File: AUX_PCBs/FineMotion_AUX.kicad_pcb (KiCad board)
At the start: 2 copper layers, 49.9 x 19.4 mm, 14 parts, among them J2 Conn_01x04_Female, U1 ME6211C, U9 MPU-9250

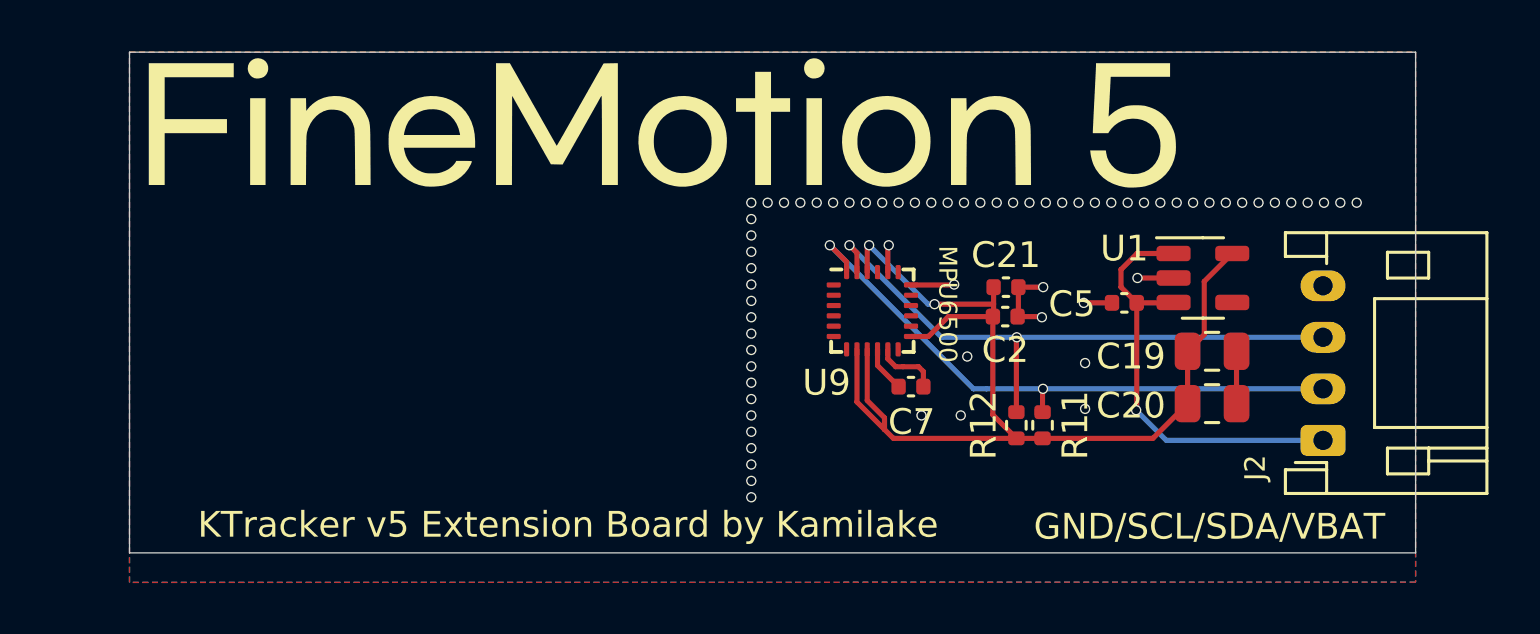
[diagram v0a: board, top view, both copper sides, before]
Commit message: Placement of pads to assemble the BNO085 module
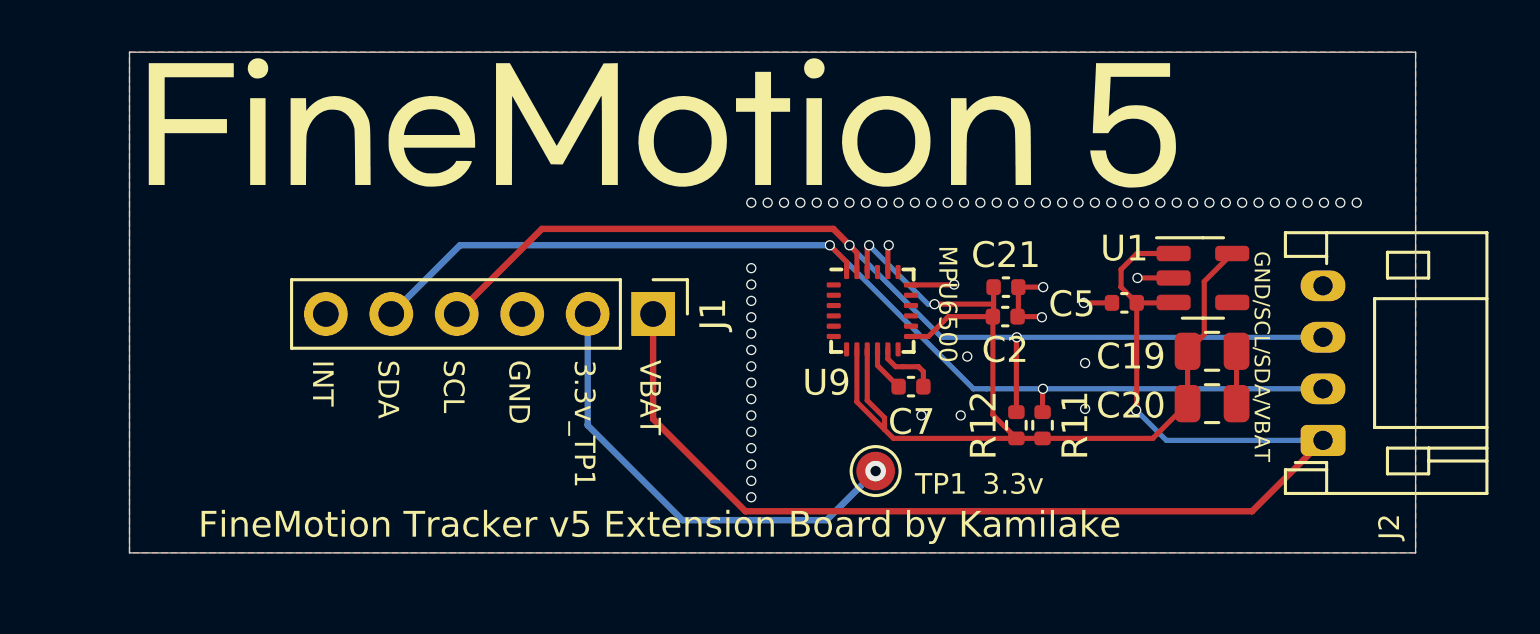
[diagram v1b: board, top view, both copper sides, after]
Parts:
- added J1: Conn_01x06_Male, Connector_PinHeader_2.54mm:PinHeader_1x06_P2.54mm_Vertical, F.Cu at (110.5, 65.9)
- added TP1: I2C_PULLUP, TestPoint:TestPoint_Pad_D1.5mm, F.Cu at (119.1, 72.0)
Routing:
- net VBAT: track 17.2 -> 49.9 mm
- net SDA: track 23.7 -> 41.8 mm
- net Net-(J1-Pad2): track 0.00 -> 17.8 mm, vias 0 -> 1
- net SCL: track 23.9 -> 40.8 mm
- net GND: vias 67 -> 64
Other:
- board text added: "3.3v"
- board text added: "3.3v_TP1"
- board text added: "FineMotion Tracker v5 Extension Board by Kamilake"
- board text added: "GND"
- board text added: "INT"
- board text added: "SCL"
- board text added: "SDA"
- board text added: "VBAT"
- board text removed: "KTracker v5 Extension Board by Kamilake"

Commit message: Premium logo~
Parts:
- G***: value LOGO -> FineMotion5
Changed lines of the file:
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@@
       (effects (font (size 1.524 1.524) (thickness 0.3)))
     )
-    (fp_text value "LOGO" (at 0.75 0) (layer "F.Adhes") hide
+    (fp_text value "FineMotion5" (at 0.75 0) (layer "F.SilkS") hide
       (effects (font (size 1.524 1.524) (thickness 0.3)))
     )
@@
         (xy 16.933333 -2.240139)
         (xy 19.808472 -2.240139)
-      ) (layer "F.SilkS") (width 0) (fill solid))
+      ) (layer "F.Mask") (width 0) (fill solid))
     (fp_poly (pts
         (xy -15.292917 2.487083)
@@
         (xy -15.892639 -0.881945)
         (xy -15.292917 -0.881945)
-      ) (layer "F.SilkS") (width 0) (fill solid))
+      ) (layer "F.Mask") (width 0) (fill solid))
     (fp_poly (pts
         (xy 1.142024 -0.954211)
@@
         (xy 0.742736 -0.959994)
         (xy 0.948969 -0.968346)
-      ) (layer "F.SilkS") (width 0) (fill solid))
+      ) (layer "F.Mask") (width 0) (fill solid))
     (fp_poly (pts
         (xy -8.663804 -0.959525)
@@
         (xy -9.128181 -0.944226)
         (xy -8.896952 -0.966529)
-      ) (layer "F.SilkS") (width 0) (fill solid))
+      ) (layer "F.Mask") (width 0) (fill solid))
     (fp_poly (pts
         (xy -12.428672 -0.960067)
@@
         (xy -12.847275 -0.945323)
         (xy -12.639255 -0.966713)
-      ) (layer "F.SilkS") (width 0) (fill solid))
+      ) (layer "F.Mask") (width 0) (fill solid))
     (fp_poly (pts
         (xy 6.087764 -2.422808)
@@
         (xy 5.8616 -2.409532)
         (xy 5.976982 -2.431571)
-      ) (layer "F.SilkS") (width 0) (fill solid))
+      ) (layer "F.Mask") (width 0) (fill solid))
     (fp_poly (pts
         (xy 4.321528 -0.881945)
@@
         (xy 3.704166 -1.905)
         (xy 4.321528 -1.905)
-      ) (layer "F.SilkS") (width 0) (fill solid))
+      ) (layer "F.Mask") (width 0) (fill solid))
     (fp_poly (pts
         (xy -15.464162 -2.413877)
@@
         (xy -15.679201 -2.423484)
         (xy -15.573337 -2.433016)
-      ) (layer "F.SilkS") (width 0) (fill solid))
+      ) (layer "F.Mask") (width 0) (fill solid))
     (fp_poly (pts
         (xy 13.200633 -0.960067)
@@
         (xy 12.78203 -0.945323)
         (xy 12.99005 -0.966713)
-      ) (layer "F.SilkS") (width 0) (fill solid))
+      ) (layer "F.Mask") (width 0) (fill solid))
     (fp_poly (pts
         (xy -16.527639 -1.693334)
@@
         (xy -19.826111 -2.240139)
         (xy -16.527639 -2.240139)
-      ) (layer "F.SilkS") (width 0) (fill solid))
+      ) (layer "F.Mask") (width 0) (fill solid))
     (fp_poly (pts
         (xy 9.044247 -0.954211)
@@
         (xy 8.644958 -0.959994)
         (xy 8.851191 -0.968346)
-      ) (layer "F.SilkS") (width 0) (fill solid))
+      ) (layer "F.Mask") (width 0) (fill solid))
     (fp_poly (pts
         (xy -1.622778 2.487083)
@@
         (xy -1.89994 -2.236178)
         (xy -1.622778 -2.241035)
-      ) (layer "F.SilkS") (width 0) (fill solid))
+      ) (layer "F.Mask") (width 0) (fill solid))
     (fp_poly (pts
         (xy 6.297083 2.487083)
@@
         (xy 5.697361 -0.881945)
         (xy 6.297083 -0.881945)
-      ) (layer "F.SilkS") (width 0) (fill solid))
+      ) (layer "F.Mask") (width 0) (fill solid))
   )
   (footprint "Capacitor_SMD:C_0402_1005Metric" (layer "F.Cu")

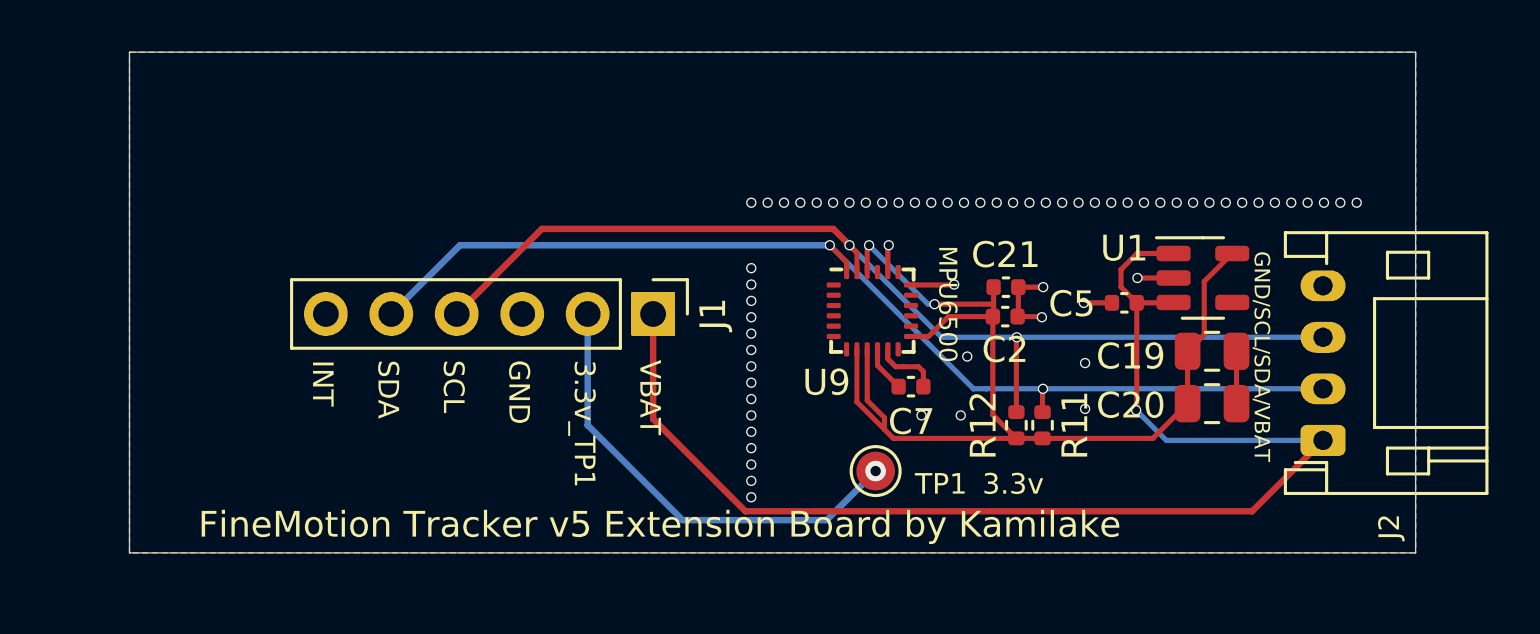
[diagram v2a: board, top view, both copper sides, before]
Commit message: Update manufacturing date
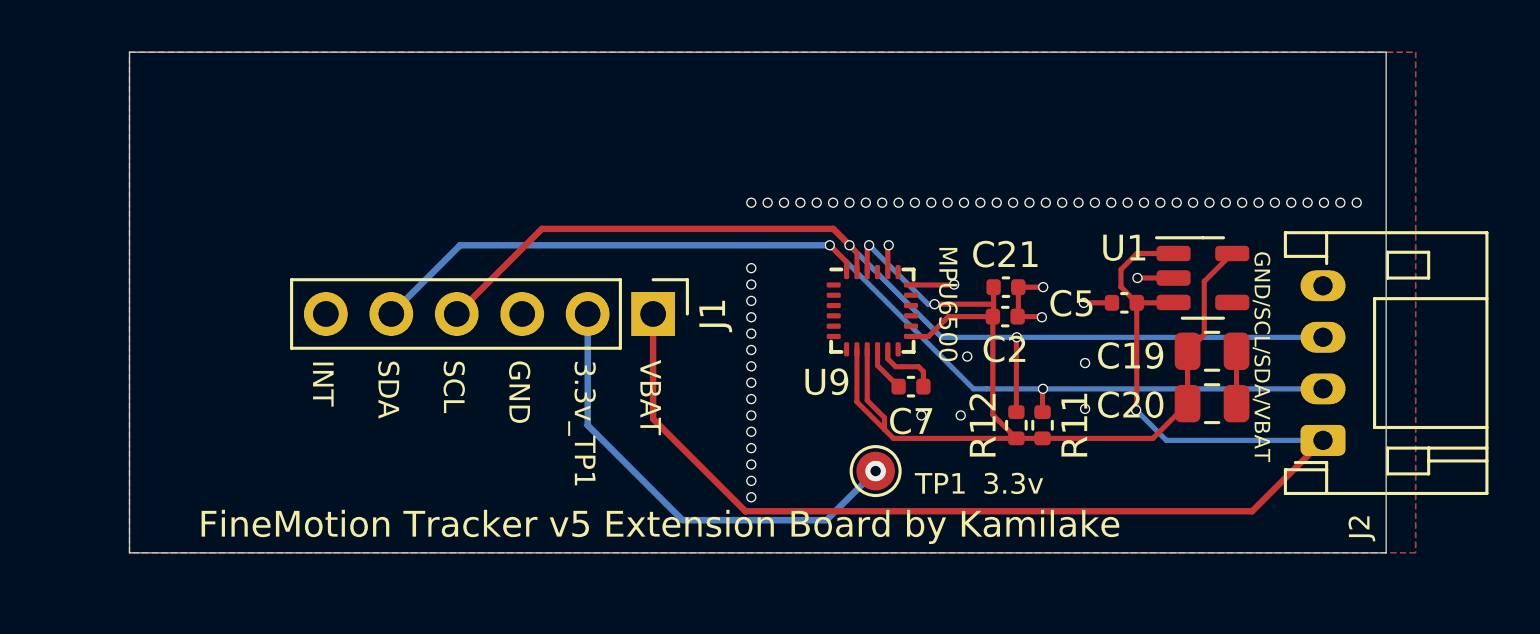
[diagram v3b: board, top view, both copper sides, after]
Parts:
- moved G*** 0.60 mm to (98.8, 67.6)
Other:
- board size 49.9 x 19.4 mm -> 48.8 x 19.4 mm
- board text added: "2023-02-09 FineMotion"
- board text added: "https://github.com/Kamilake/FineMotion-Tracker"
- board text removed: "2022-09-24 KTracker v5"
- board text removed: "https://github.com/Kamilake/KTracker-SlimeVR-PCB"
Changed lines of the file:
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@@
     (property "Sheetname" "")
     (attr through_hole)
-    (fp_text reference "J2" (at -3.35 2.577 90) (layer "F.SilkS")
+    (fp_text reference "J2" (at -3.35 1.434 90) (layer "F.SilkS")
       (effects (font (size 0.8 0.8) (thickness 0.15)))
     )
-    (fp_text value "Conn_01x04_Female" (at 3 7.45 90) (layer "F.Fab")
+    (fp_text value "Conn_01x04_Female" (at 3 7.45 90) (layer "F.Fab") hide
       (effects (font (size 1 1) (thickness 0.15)))
     )
@@
   )
   (footprint "kamilib:sleepy300dpi" (layer "B.Cu")
-    (at 98.84 68.16 180)
+    (at 98.806 67.564 180)
     (attr through_hole)
     (fp_text reference "G***" (at 0 0) (layer "B.SilkS") hide
@@
       ) (layer "B.SilkS") (width 0.01) (fill solid))
   )
-  (gr_line (start 90.17 55.753) (end 140.081 55.753) (layer "Edge.Cuts") (width 0.05))
-  (gr_line (start 140.081 55.753) (end 140.081 75.184) (layer "Edge.Cuts") (width 0.05))
-  (gr_line (start 140.081 75.184) (end 90.17 75.184) (layer "Edge.Cuts") (width 0.05))
+  (gr_line (start 90.17 55.753) (end 138.938 55.753) (layer "Edge.Cuts") (width 0.05))
+  (gr_line (start 138.938 55.753) (end 138.938 75.184) (layer "Edge.Cuts") (width 0.05))
+  (gr_line (start 138.938 75.184) (end 90.17 75.184) (layer "Edge.Cuts") (width 0.05))
   (gr_line (start 90.17 75.184) (end 90.17 55.753) (layer "Edge.Cuts") (width 0.05))
-  (gr_text "https://github.com/Kamilake/KTracker-SlimeVR-PCB" (at 107.9246 58.547) (layer "B.SilkS")
+  (gr_text "https://github.com/Kamilake/FineMotion-Tracker" (at 106.807 58.547) (layer "B.SilkS")
     (effects (font (size 0.8 0.8) (thickness 0.13)) (justify mirror))
   )
-  (gr_text "2022-09-24 KTracker v5" (at 100.2792 56.9722) (layer "B.SilkS")
+  (gr_text "2023-02-09 FineMotion" (at 99.949 56.9722) (layer "B.SilkS")
     (effects (font (size 0.9 0.9) (thickness 0.14)) (justify mirror))
   )
